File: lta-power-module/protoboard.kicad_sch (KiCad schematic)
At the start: 192 parts

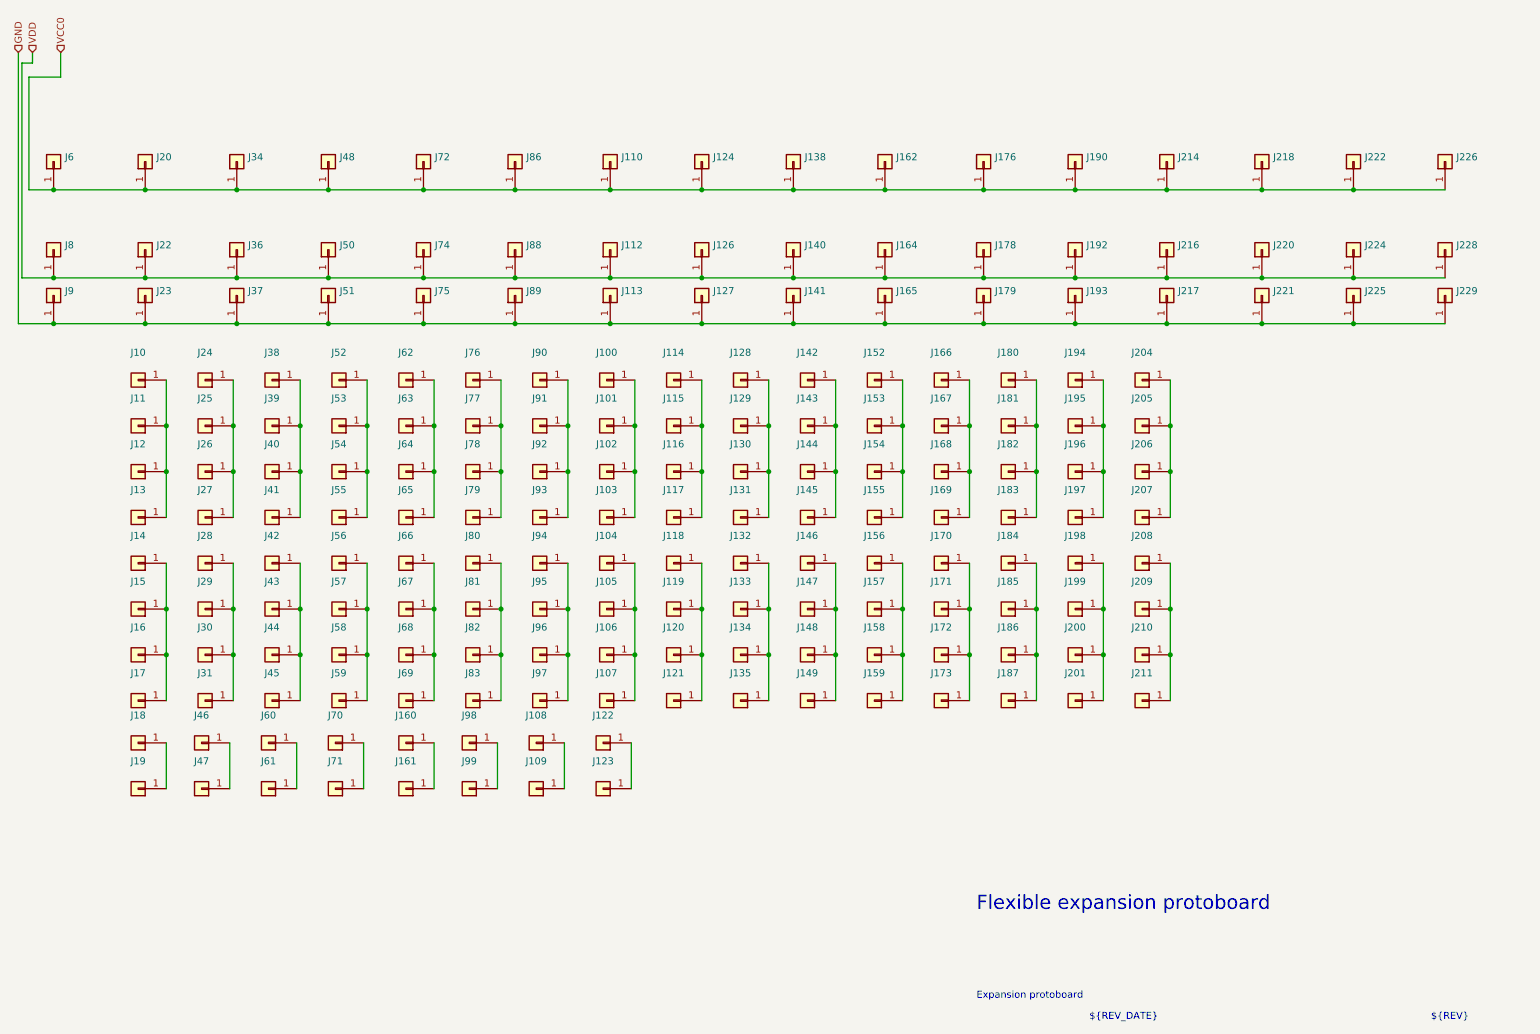
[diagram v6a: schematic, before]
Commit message: Update module footprints to be more accurate.
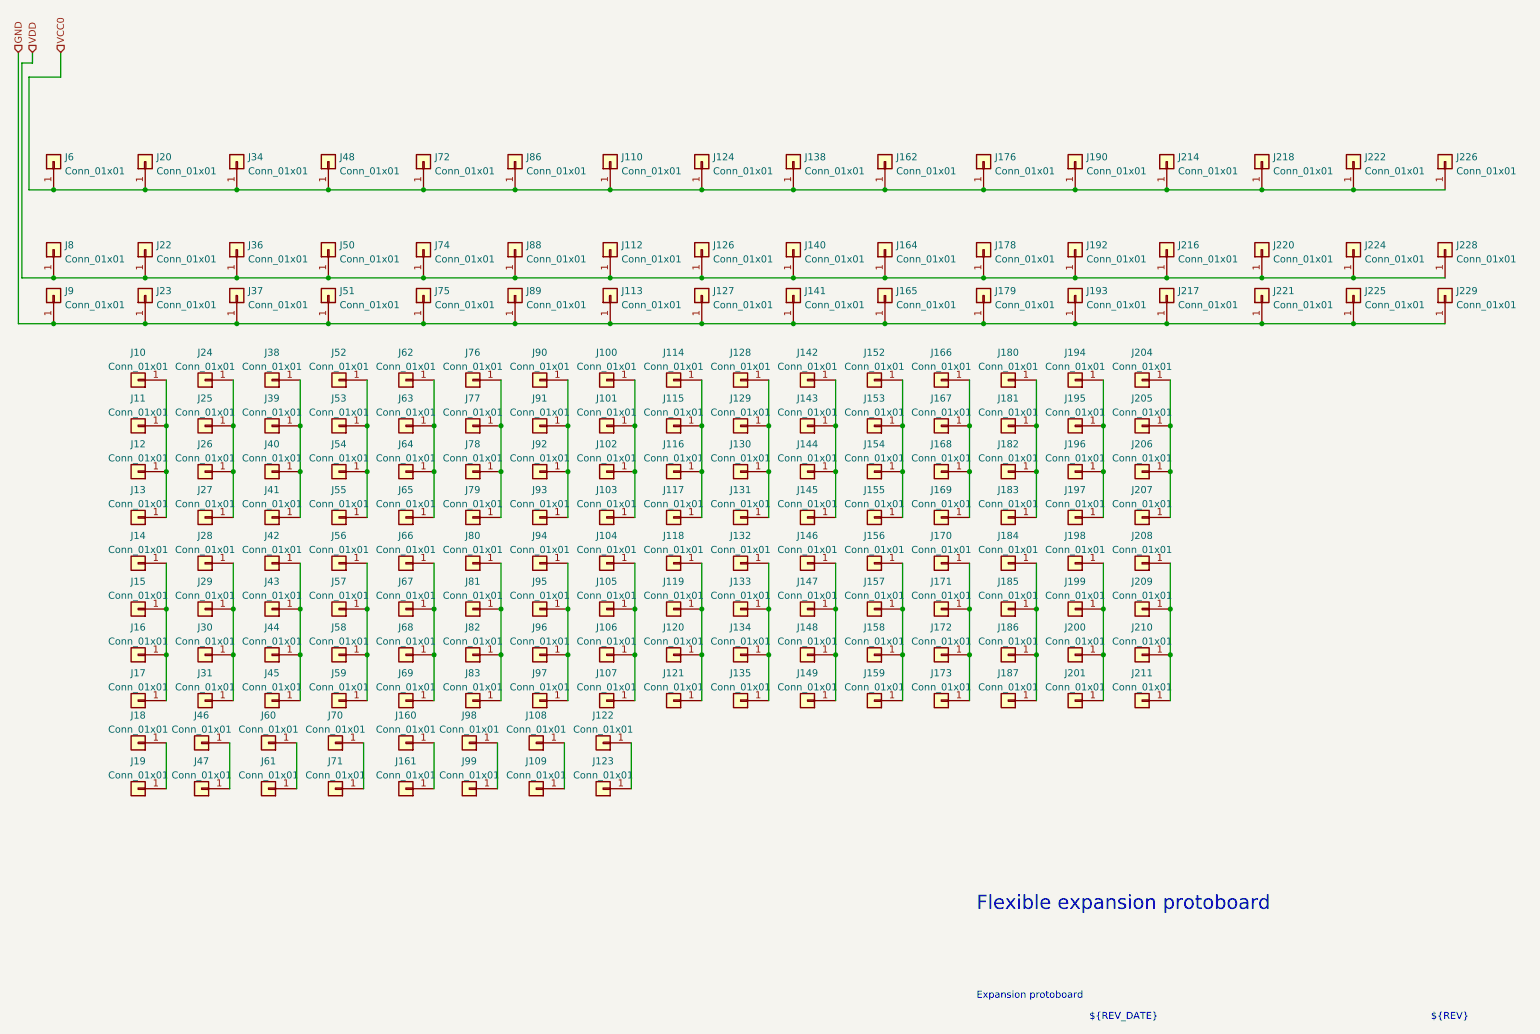
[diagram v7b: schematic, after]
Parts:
- J10, J100, J101, J102, J103, J104, J105, J106, J107, J109, J11, J110, J112, J113, J114, J115, J116, J117, J118, J119, J12, J120, J121, J123, J124, J126, J127, J128, J129, J13, J130, J131, J132, J133, J134, J135, J138, J14, J140, J141, J142, J143, J144, J145, J146, J147, J148, J149, J15, J152, J153, J154, J155, J156, J157, J158, J159, J16, J161, J162, J164, J165, J166, J167, J168, J169, J17, J170, J171, J172, J173, J176, J178, J179, J180, J181, J182, J183, J184, J185, J186, J187, J19, J190, J192, J193, J194, J195, J196, J197, J198, J199, J20, J200, J201, J204, J205, J206, J207, J208, J209, J210, J211, J214, J216, J217, J218, J22, J220, J221, J222, J224, J225, J226, J228, J229, J23, J24, J25, J26, J27, J28, J29, J30, J31, J34, J36, J37, J38, J39, J40, J41, J42, J43, J44, J45, J47, J48, J50, J51, J52, J53, J54, J55, J56, J57, J58, J59, J6, J61, J62, J63, J64, J65, J66, J67, J68, J69, J71, J72, J74, J75, J76, J77, J78, J79, J8, J80, J81, J82, J83, J86, J88, J89, J9, J90, J91, J92, J93, J94, J95, J96, J97, J99: value (none) -> Conn_01x01; footprint (none) -> Aaron_Pads:1mm_PTH_No_Silk
- J108, J122, J160, J18, J46, J60, J70, J98: value (none) -> Conn_01x01; footprint (none) -> Aaron_Pads:1.6mm_PTH_No_Silk
